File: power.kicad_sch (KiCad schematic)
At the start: 10 parts, among them J20 Screw_Terminal_01x02, U6 AMS1117-3.3

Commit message: cleanup, ready to submit.
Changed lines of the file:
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@@
 					(size 1.27 1.27)
 				)
+				(hide yes)
 			)
 		)
@@
 					(size 1.27 1.27)
 				)
+				(hide yes)
 			)
 		)
@@
 					(size 1.27 1.27)
 				)
+				(hide yes)
 			)
 		)
@@
 					(size 1.27 1.27)
 				)
+				(hide yes)
 			)
 		)
@@
 			)
 		)
-		(property "Description" "Generic screw terminal, single row, 01x02, script generated (kicad-library-utils/schlib/autogen/connector/)"
+		(property "Description" "Generic screw terminal, 01x02"
 			(at 152.4 68.58 0)
 			(effects
@@
 					(size 1.27 1.27)
 				)
+				(hide yes)
 			)
 		)
@@
 					(size 1.27 1.27)
 				)
+				(hide yes)
 			)
 		)
@@
 					(size 1.27 1.27)
 				)
+				(hide yes)
 			)
 		)
@@
 					(size 1.27 1.27)
 				)
+				(hide yes)
 			)
 		)
@@
 					(size 1.27 1.27)
 				)
-			)
-		)
+				(hide yes)
+			)
+		)

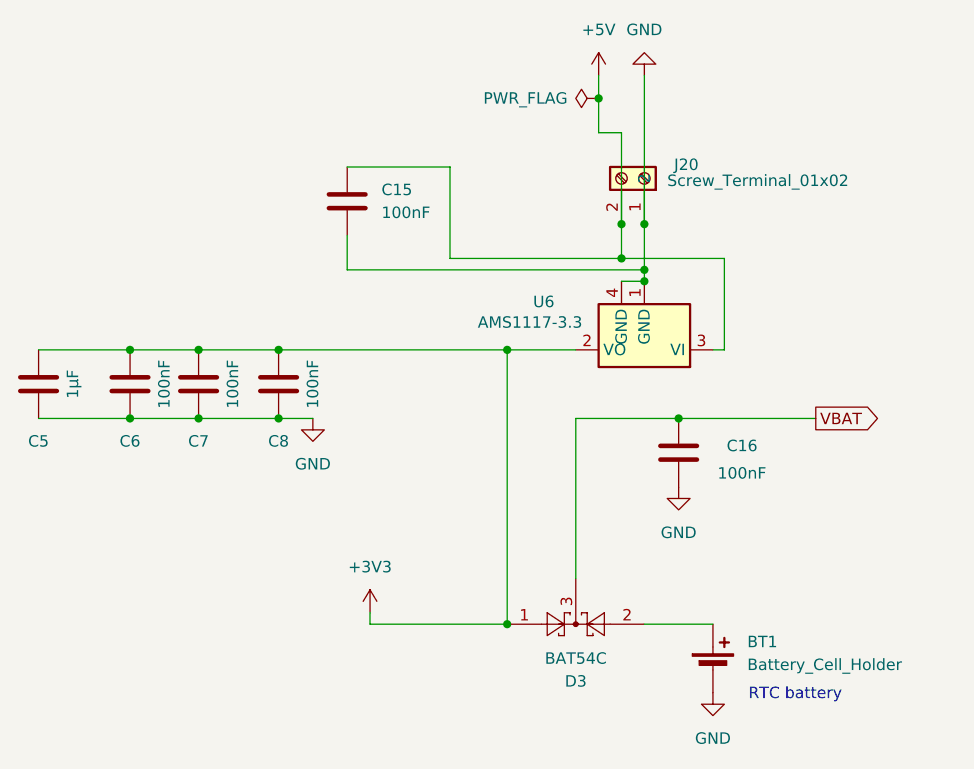
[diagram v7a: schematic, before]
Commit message: As made,  t16-F411 v0.2.0 2025-05, with added notes about needed fixes and results from some testing.
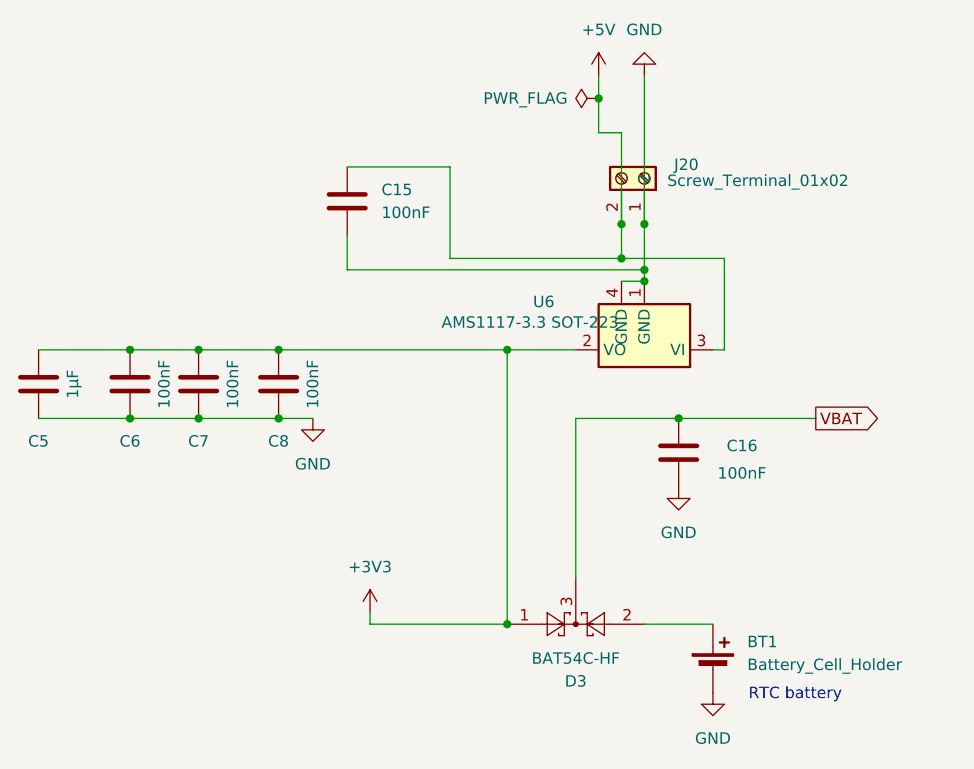
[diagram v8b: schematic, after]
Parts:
- C15, C16, C6, C7, C8: Manufacturer (none) -> Samsung; MfgPart (none) -> CL10B104KB8NNNC
- C5: Manufacturer (none) -> Samsung; MfgPart (none) -> CL10A105KA8NNNC
- D3: value BAT54C -> BAT54C-HF; Manufacturer Diodes Inc. -> Comchip Technology; MfgPart BAT54C -> BAT54C-HF
- U6: value AMS1117-3.3 -> AMS1117-3.3 SOT-223
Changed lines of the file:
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@@
 			)
 		)
-		(property "Value" "AMS1117-3.3"
+		(property "Value" "AMS1117-3.3 SOT-223"
 			(at 139.7 84.582 0)
 			(effects
@@
 			)
 		)
-		(property "Datasheet" "~"
+		(property "Datasheet" ""
 			(at 111.76 91.44 0)
 			(effects
@@
 		)
 		(property "pads" "2"
+			(at 111.76 91.44 0)
+			(effects
+				(font
+					(size 1.27 1.27)
+				)
+				(hide yes)
+			)
+		)
+		(property "Manufacturer" "Samsung"
+			(at 111.76 91.44 0)
+			(effects
+				(font
+					(size 1.27 1.27)
+				)
+				(hide yes)
+			)
+		)
+		(property "MfgPart" "CL10B104KB8NNNC"
 			(at 111.76 91.44 0)
 			(effects
@@
 			)
 		)
-		(property "Datasheet" "~"
+		(property "Datasheet" ""
 			(at 102.87 91.44 0)
 			(effects
@@
 		)
 		(property "pads" "2"
+			(at 102.87 91.44 0)
+			(effects
+				(font
+					(size 1.27 1.27)
+				)
+				(hide yes)
+			)
+		)
+		(property "Manufacturer" "Samsung"
+			(at 102.87 91.44 0)
+			(effects
+				(font
+					(size 1.27 1.27)
+				)
+				(hide yes)
+			)
+		)
+		(property "MfgPart" "CL10B104KB8NNNC"
 			(at 102.87 91.44 0)
 			(effects
@@
 			)
 		)
-		(property "Datasheet" "~https://www.te.com/commerce/DocumentDelivery/DDEController?Action=srchrtrv&DocNm=BAT-HLD-012-SMT&DocType=Data+Sheet&DocLang=English&DocFormat=pdf&PartCntxt=BAT-HLD-012-SMT"
+		(property "Datasheet" "https://www.te.com/commerce/DocumentDelivery/DDEController?Action=srchrtrv&DocNm=BAT-HLD-012-SMT&DocType=Data+Sheet&DocLang=English&DocFormat=pdf&PartCntxt=BAT-HLD-012-SMT"
 			(at 160.02 121.666 90)
 			(effects
@@
 			)
 		)
-		(property "Datasheet" "~"
+		(property "Datasheet" ""
 			(at 152.4 68.58 0)
 			(effects
@@
 			)
 		)
-		(property "Datasheet" "~"
+		(property "Datasheet" ""
 			(at 85.09 91.44 0)
 			(effects
@@
 		)
 		(property "pads" "2"
+			(at 85.09 91.44 0)
+			(effects
+				(font
+					(size 1.27 1.27)
+				)
+				(hide yes)
+			)
+		)
+		(property "Manufacturer" "Samsung"
+			(at 85.09 91.44 0)
+			(effects
+				(font
+					(size 1.27 1.27)
+				)
+				(hide yes)
+			)
+		)
+		(property "MfgPart" "CL10A105KA8NNNC"
 			(at 85.09 91.44 0)
 			(effects
@@
 			)
 		)
-		(property "Value" "BAT54C"
+		(property "Value" "BAT54C-HF"
 			(at 144.78 121.92 0)
 			(effects
@@
 			)
 		)
-		(property "Datasheet" "http://www.diodes.com/_files/datasheets/ds11005.pdf"
+		(property "Datasheet" "https://www.comchiptech.com/admin/files/product/QW-JB083%20BAT54-HF%20Series%20RevA.pdf"
 			(at 142.748 118.11 0)
 			(effects
@@
 			)
 		)
-		(property "Manufacturer" "Diodes Inc."
+		(property "Manufacturer" "Comchip Technology"
 			(at 144.78 118.11 0)
 			(effects
@@
 			)
 		)
-		(property "MfgPart" "BAT54C"
+		(property "MfgPart" "BAT54C-HF"
 			(at 144.78 118.11 0)
 			(effects
@@
 			)
 		)
-		(property "Datasheet" "~"
+		(property "Datasheet" ""
 			(at 156.21 99.06 0)
 			(effects
@@
 		)
 		(property "pads" "2"
+			(at 156.21 99.06 0)
+			(effects
+				(font
+					(size 1.27 1.27)
+				)
+				(hide yes)
+			)
+		)
+		(property "Manufacturer" "Samsung"
+			(at 156.21 99.06 0)
+			(effects
+				(font
+					(size 1.27 1.27)
+				)
+				(hide yes)
+			)
+		)
+		(property "MfgPart" "CL10B104KB8NNNC"
 			(at 156.21 99.06 0)
 			(effects
@@
 			)
 		)
-		(property "Datasheet" "~"
+		(property "Datasheet" ""
 			(at 119.38 71.12 0)
 			(effects
@@
 		)
 		(property "pads" "2"
+			(at 119.38 71.12 0)
+			(effects
+				(font
+					(size 1.27 1.27)
+				)
+				(hide yes)
+			)
+		)
+		(property "Manufacturer" "Samsung"
+			(at 119.38 71.12 0)
+			(effects
+				(font
+					(size 1.27 1.27)
+				)
+				(hide yes)
+			)
+		)
+		(property "MfgPart" "CL10B104KB8NNNC"
 			(at 119.38 71.12 0)
 			(effects
@@
 			)
 		)
-		(property "Datasheet" "~"
+		(property "Datasheet" ""
 			(at 95.25 91.44 0)
 			(effects
@@
 			(at 95.25 91.44 0)
 			(effects
+				(font
+					(size 1.27 1.27)
+				)
+				(hide yes)
+			)
+		)
+		(property "Manufacturer" "Samsung"
+			(at 95.25 91.44 0)
+			(effects
+				(font
+					(size 1.27 1.27)
+				)
+				(hide yes)
+			)
+		)
+		(property "MfgPart" "CL10B104KB8NNNC"
+			(at 95.25 91.44 0)
+			(effects
